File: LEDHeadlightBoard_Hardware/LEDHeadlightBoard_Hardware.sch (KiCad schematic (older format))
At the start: 5 parts, among them J1 Solder_Pad, J2 Solder_Pad

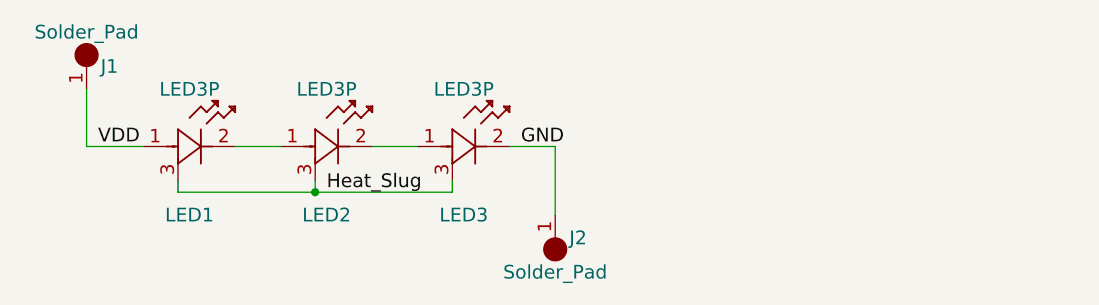
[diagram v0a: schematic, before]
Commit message: Board Complete for Cree XLamp XP-G2
EasyEDA does not like the gerbs, need to figure that out. May have to do with how small the board is.
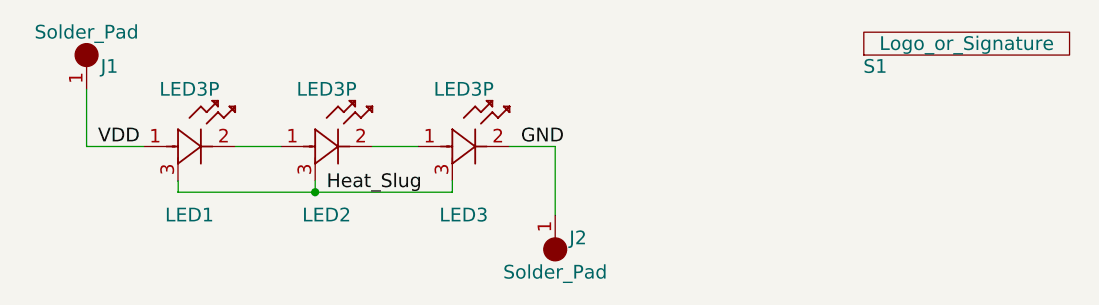
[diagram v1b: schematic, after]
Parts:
- added S1: Logo_or_Signature, MRDT_Silkscreens:MRDT_Logo_10mm, symbol Logo_or_Signature
- J1, J2: footprint MRDT-Connectors:Solder_Pad_6mmX4mm -> MRDT-Connectors:Solder_Pad_5mmX3mm
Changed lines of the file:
@@
 LIBS:contrib
 LIBS:valves
-LIBS:MRDT-Actives
-LIBS:MRDT-Connectors
-LIBS:MRDT-Devices
-LIBS:MRDT-Drill_Holes
-LIBS:MRDT-Headers
-LIBS:MRDT-ICs
-LIBS:MRDT-Passives
-LIBS:MRDT-Shields
-LIBS:MRDT-Silkscreens
-LIBS:MRDT-Switches
+LIBS:MRDT_Actives
+LIBS:MRDT_Connectors
+LIBS:MRDT_Devices
+LIBS:MRDT_Drill_Holes
+LIBS:MRDT_Headers
+LIBS:MRDT_ICs
+LIBS:MRDT_Passives
+LIBS:MRDT_Shields
+LIBS:MRDT_Silkscreens
+LIBS:MRDT_Switches
 LIBS:LEDHeadlightBoard_Hardware-cache
 EELAYER 25 0
@@
 F 0 "J1" H 1250 1350 60  0000 C CNN
 F 1 "Solder_Pad" H 1150 1500 60  0000 C CNN
-F 2 "MRDT-Connectors:Solder_Pad_6mmX4mm" H 1150 1200 60  0001 C CNN
+F 2 "MRDT-Connectors:Solder_Pad_5mmX3mm" H 1150 1200 60  0001 C CNN
 F 3 "" H 1150 1200 60  0001 C CNN
 	1    1150 1200
@@
 F 0 "J2" H 3100 1800 60  0000 C CNN
 F 1 "Solder_Pad" H 3200 1950 60  0000 C CNN
-F 2 "MRDT-Connectors:Solder_Pad_6mmX4mm" H 3200 1650 60  0001 C CNN
+F 2 "MRDT-Connectors:Solder_Pad_5mmX3mm" H 3200 1650 60  0001 C CNN
 F 3 "" H 3200 1650 60  0001 C CNN
 	1    3200 1650
@@
 Text Label 1200 1400 0    60   ~ 0
 VDD
+$Comp
+L Logo_or_Signature S1
+U 1 1 5AB0B18A
+P 4550 1000
+F 0 "S1" H 4600 950 60  0000 C CNN
+F 1 "Logo_or_Signature" H 5000 1050 60  0000 C CNN
+F 2 "MRDT_Silkscreens:MRDT_Logo_10mm" H 4550 1000 60  0001 C CNN
+F 3 "" H 4550 1000 60  0001 C CNN
+	1    4550 1000
+	1    0    0    -1
+$EndComp
 $EndSCHEMATC
